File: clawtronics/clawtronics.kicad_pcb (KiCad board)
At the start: 4 copper layers, 68.5 x 87.6 mm, 76 parts, among them J1 Screw_Terminal_01x05, J11 Screw_Terminal_01x02, J2 DX07S016JA3R1500, J4 Screw_Terminal_01x09, J5 Screw_Terminal_01x04, J6 Conn_01x16_Pin, M1 Motor_DC, M2 Motor_DC, M3 Motor_DC, Q2 AO3400A, SW1 SW_SPST_TS-1088-xR020, SW2 SW_SPST_TS-1088-xR020, U1 ESP32-S3-WROOM-1, U2 LD1117S33TR_SOT223, U5 DRV8876PWPR, U7 DRV8876PWPR, U8 DRV8876PWPR, U9 74LVC1G17

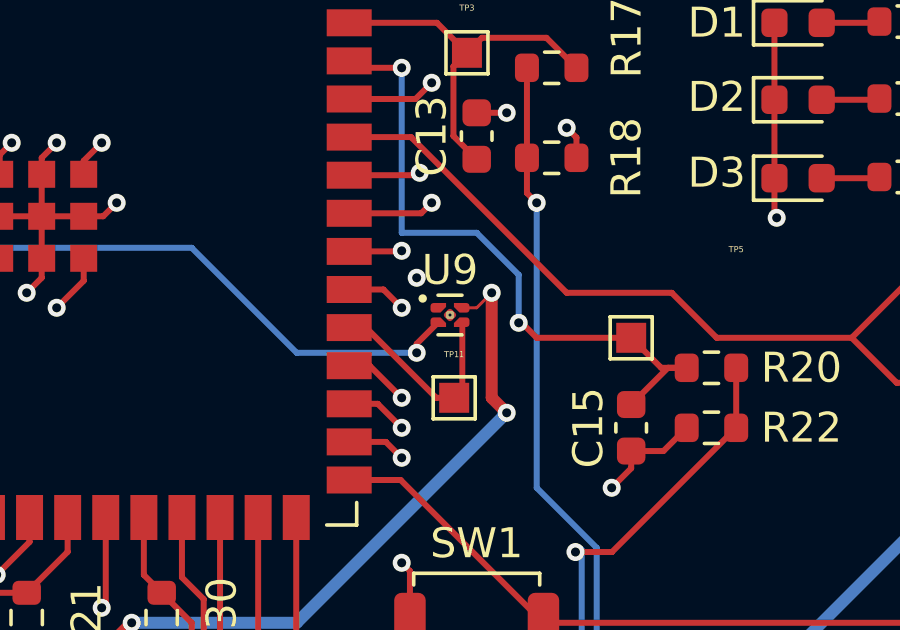
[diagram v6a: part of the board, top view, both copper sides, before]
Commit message: update BOM with PNs
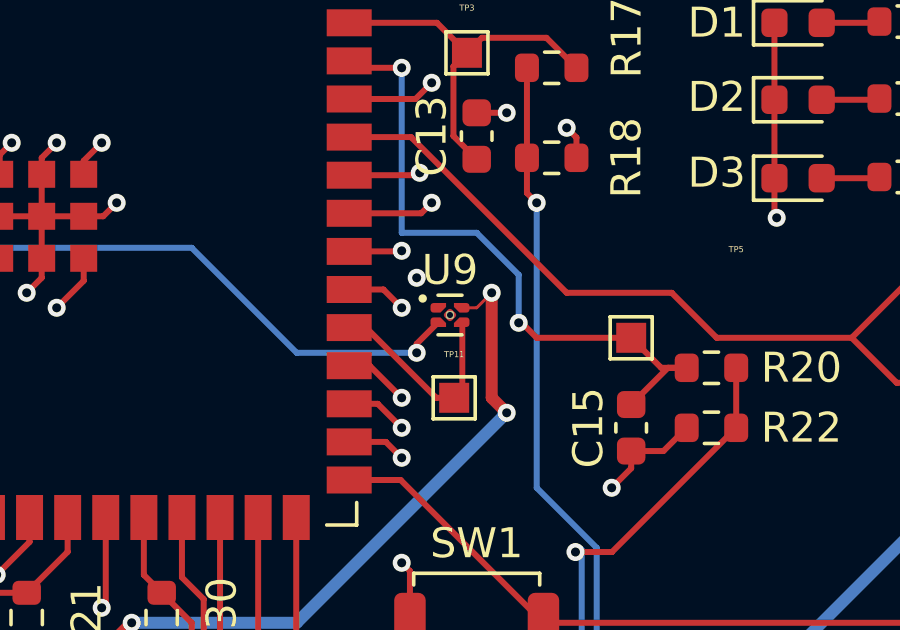
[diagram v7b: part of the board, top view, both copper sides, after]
